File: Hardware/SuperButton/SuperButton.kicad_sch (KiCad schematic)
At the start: 0 parts

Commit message: Add switches
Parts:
- added C103: 5pf, Capacitor_SMD:C_0805_2012Metric, symbol Device:C_Small
- added C104: 0.1uf, Capacitor_SMD:C_0805_2012Metric, symbol Device:C_Small
- added D101, D102: 3.6 Zener, Diode_SMD:D_0805_2012Metric, symbol Device:D_Zener
- added D103: SDI, LED_SMD:LED_0805_2012Metric, symbol Device:LED
- added D104: PWR, LED_SMD:LED_0805_2012Metric, symbol Device:LED
- added J101: USBC, Connector_USB:USB_C_Receptacle_XKB_U262-16XN-4BVC11, symbol Connector:USB_C_Receptacle_USB2.0
- added J103: ICSP, Connector:Tag-Connect_TC2050-IDC-FP_2x05_P1.27mm_Vertical, symbol Connector_Generic:Conn_02x05_Odd_Even
- added R101, R102: 5K1, Resistor_SMD:R_0805_2012Metric, symbol Device:R_Small
- added R103, R105: 68R, Resistor_SMD:R_0805_2012Metric, symbol Device:R_Small
- added R104: 1K5, Resistor_SMD:R_0805_2012Metric, symbol Device:R_Small
- added R106, R107: 1K, Resistor_SMD:R_0805_2012Metric, symbol Device:R_Small
- added SW101: Switch, Switch_Keyboard_Cherry_MX:SW_Cherry_MX_PCB, symbol Switch:SW_SPST
- added U102: ATtiny85-20S, Package_SO:SOIC-8W_5.3x5.3mm_P1.27mm, symbol MCU_Microchip_ATtiny:ATtiny85-20S
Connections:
- new net: D103.1 (K), R106.2
- new net: J101.B5 (CC2), R101.2
- new net: J101.A5 (CC1), R102.2
- new net: D104.1 (K), R107.2
- new net +5V: C103.1, C104.1, D103.2 (A), D104.2 (A), J103.2 (Pin_2), R104.1, U102.8 (VCC)
- new net GND: C103.2, C104.2, D101.2 (A), D102.2 (A), J101.A1 (GND), J101.A12 (GND), J101.B1 (GND), J101.B12 (GND), J101.S1 (SHIELD), J103.10 (Pin_10), R101.1, R102.1, R107.1, SW101.2 (B), U102.4 (GND)
- new net ICSP_RST: J103.5 (Pin_5)
- new net RST: U102.1 (~{RESET}/PB5)
- new net SCK: J103.7 (Pin_7), SW101.1 (A), U102.7 (PB2)
- new net SDI: J103.9 (Pin_9), R106.1, U102.6 (PB1)
- new net SDO: J103.1 (Pin_1), U102.5 (AREF/PB0)
- new net USB+: D102.1 (K), J101.A6 (D+), J101.B6 (D+), R104.2, R105.1
- new net USB-: D101.1 (K), J101.A7 (D-), J101.B7 (D-), R103.1
- new net USBA: R105.2, U102.2 (XTAL1/PB3)
- new net USBB: R103.2, U102.3 (XTAL2/PB4)
- new net VBUS: J101.A4 (VBUS), J101.A9 (VBUS), J101.B4 (VBUS), J101.B9 (VBUS)
- no-connect marks 0 -> 6
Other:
- note added: "ICSP"
- note added: "LEDs"
- note added: "MCU"

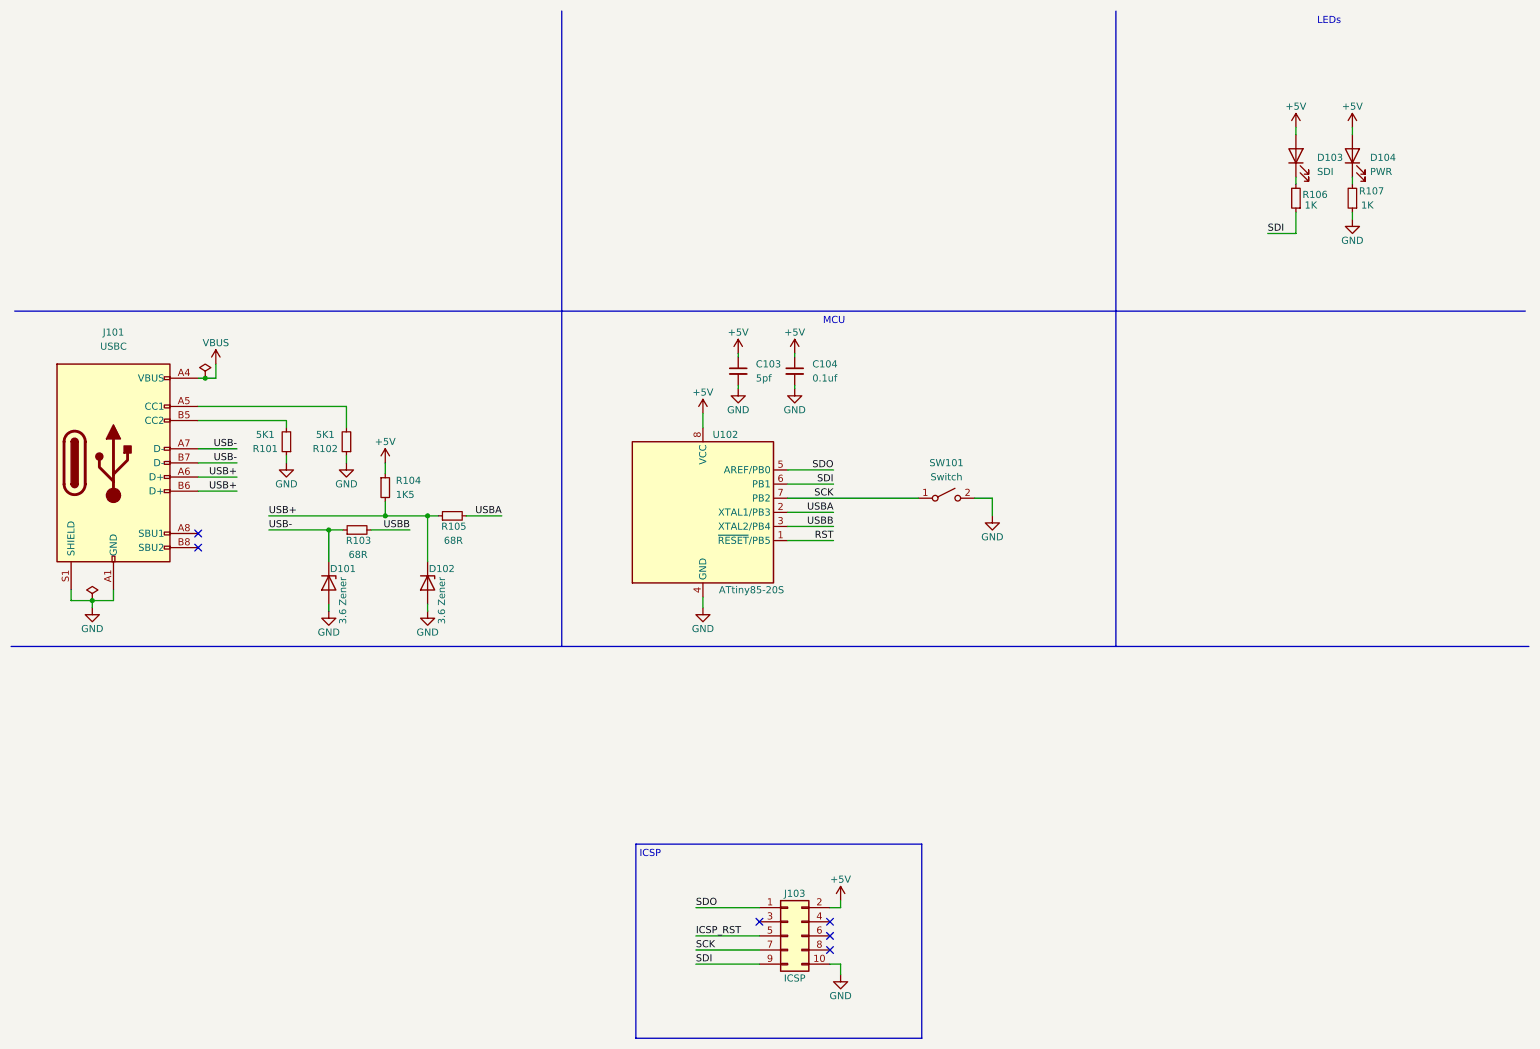
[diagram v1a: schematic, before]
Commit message: Add board outline
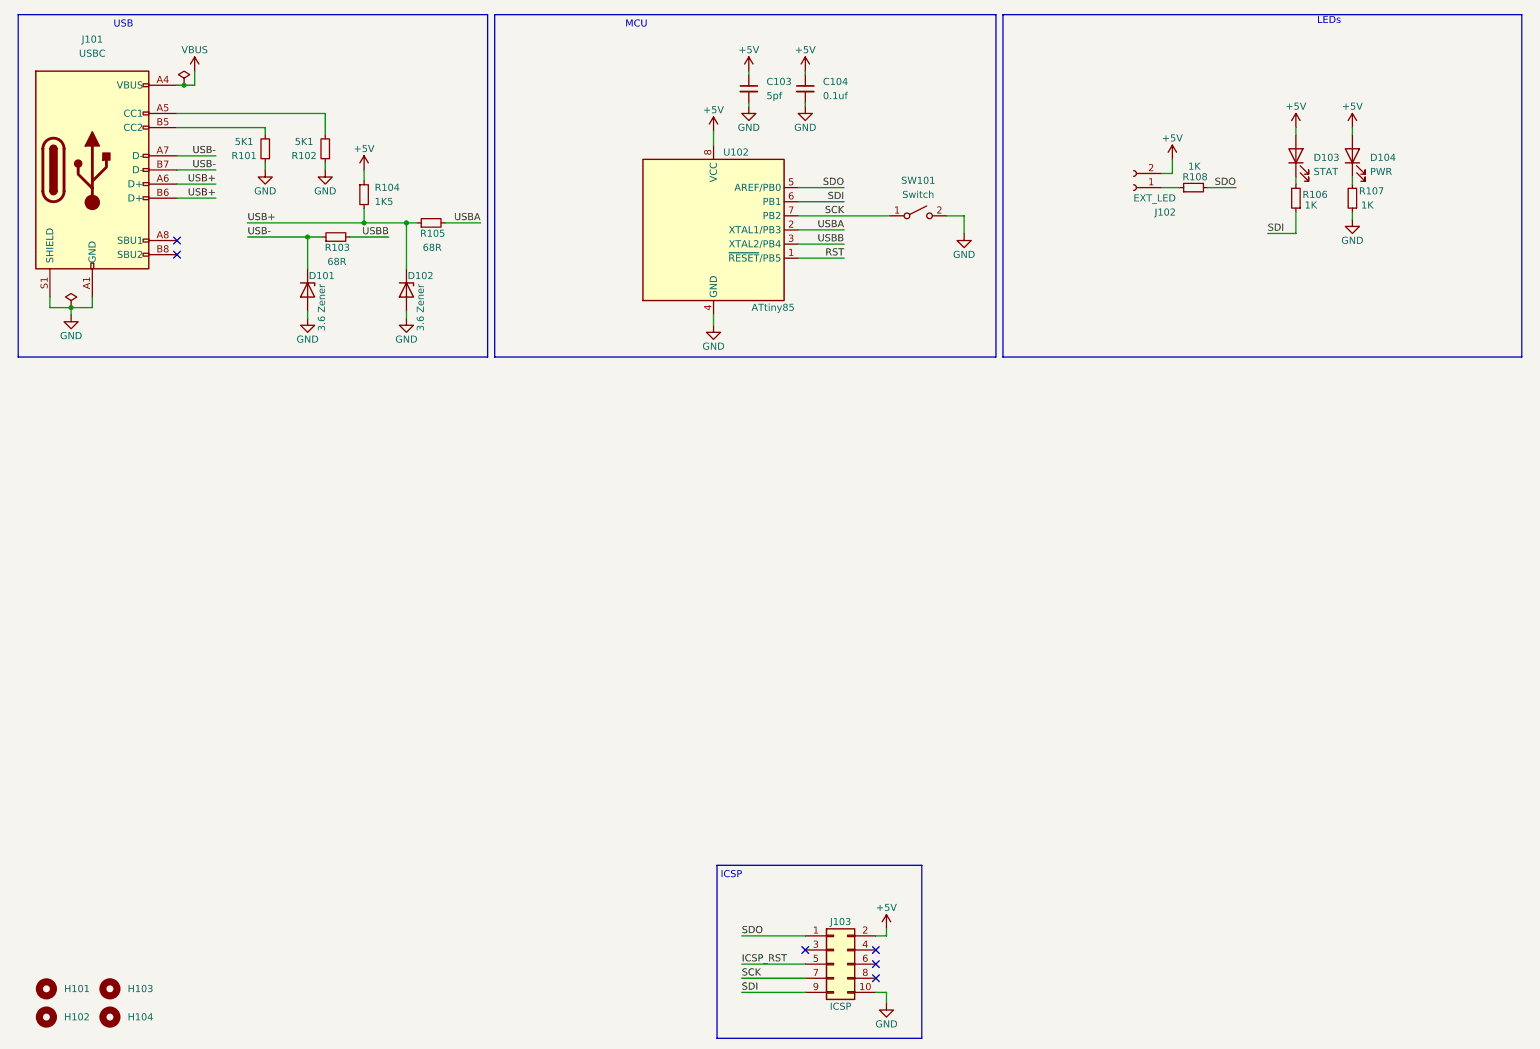
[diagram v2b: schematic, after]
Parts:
- added H101, H102, H103, H104: MountingHole, MountingHole:MountingHole_6.5mm, symbol Mechanical:MountingHole
- added J102: EXT_LED, Connector_Wire:SolderWire-0.15sqmm_1x02_P4mm_D0.5mm_OD1.5mm_Relief, symbol Connector:Conn_01x02_Female
- added R108: 1K, Resistor_SMD:R_0805_2012Metric, symbol Device:R_Small
- D103: value SDI -> STAT
- U102: value ATtiny85-20S -> ATtiny85
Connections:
- net +5V: now also J102.2 (Pin_2)
- net SDO: now also R108.2
- new net: J102.1 (Pin_1), R108.1
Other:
- note added: "USB"
- moved on the sheet: C103, C104, D101, D102, J101, J103, R101, R102, R103, R104, R105, SW101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

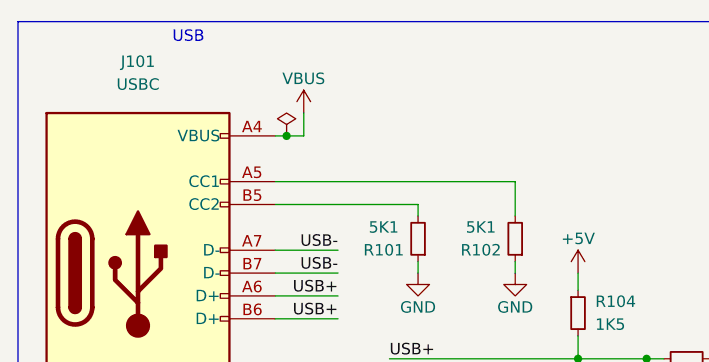
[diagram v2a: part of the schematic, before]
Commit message: Add ci/cd
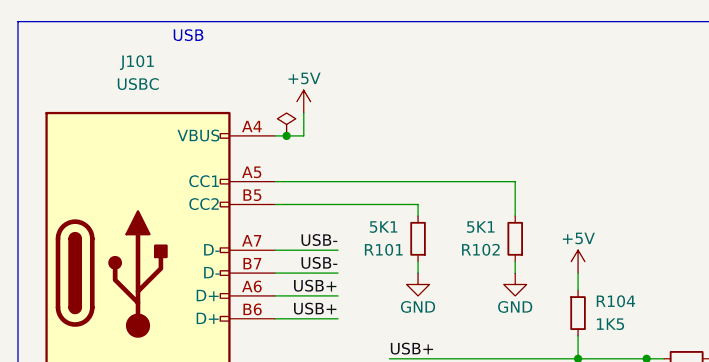
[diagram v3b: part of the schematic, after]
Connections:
- net VBUS is gone; now on net +5V: J101.A4 (VBUS), J101.A9 (VBUS), J101.B4 (VBUS), J101.B9 (VBUS)
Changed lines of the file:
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@@
+    (pin "1")
+  )
+  (symbol (lib_id "power:+5V") (at 45.085 23.495 0) (unit 1)
+    (in_bom yes) (on_board yes)
+    (property "Reference" "#PWR?" (id 0) (at 45.085 27.305 0)
+      (effects (font (size 1.27 1.27)) hide)
+    )
+    (property "Value" "+5V" (id 1) (at 45.085 19.685 0))
+    (property "Footprint" "" (id 2) (at 45.085 23.495 0)
+      (effects (font (size 1.27 1.27)) hide)
+    )
+    (property "Datasheet" "" (id 3) (at 45.085 23.495 0)
+      (effects (font (size 1.27 1.27)) hide)
+    )
     (pin "1")
   )
@@
     )
     (property "Datasheet" "" (id 3) (at 83.185 67.945 0)
-      (effects (font (size 1.27 1.27)) hide)
-    )
-    (pin "1")
-  )
-  (symbol (lib_id "power:VBUS") (at 45.085 23.495 0) (unit 1)
-    (in_bom yes) (on_board yes)
-    (property "Reference" "#PWR0117" (id 0) (at 45.085 27.305 0)
-      (effects (font (size 1.27 1.27)) hide)
-    )
-    (property "Value" "VBUS" (id 1) (at 45.085 19.685 0))
-    (property "Footprint" "" (id 2) (at 45.085 23.495 0)
-      (effects (font (size 1.27 1.27)) hide)
-    )
-    (property "Datasheet" "" (id 3) (at 45.085 23.495 0)
       (effects (font (size 1.27 1.27)) hide)
     )
@@
       (reference "#PWR0116") (unit 1) (value "GND") (footprint "")
     )
-    (path "/24487fac-3471-4a2e-a636-bc4b8b05c989"
-      (reference "#PWR0117") (unit 1) (value "VBUS") (footprint "")
-    )
     (path "/e8def7ce-3c91-44dc-84e6-03f70fae4ce8"
       (reference "#PWR0118") (unit 1) (value "GND") (footprint "")
@@
       (reference "#PWR0121") (unit 1) (value "+5V") (footprint "")
     )
+    (path "/05f1f0c0-1fb1-4746-8d9b-f5d06dd44701"
+      (reference "#PWR?") (unit 1) (value "+5V") (footprint "")
+    )
     (path "/ec261643-1568-4081-bb06-d04055847d6b"

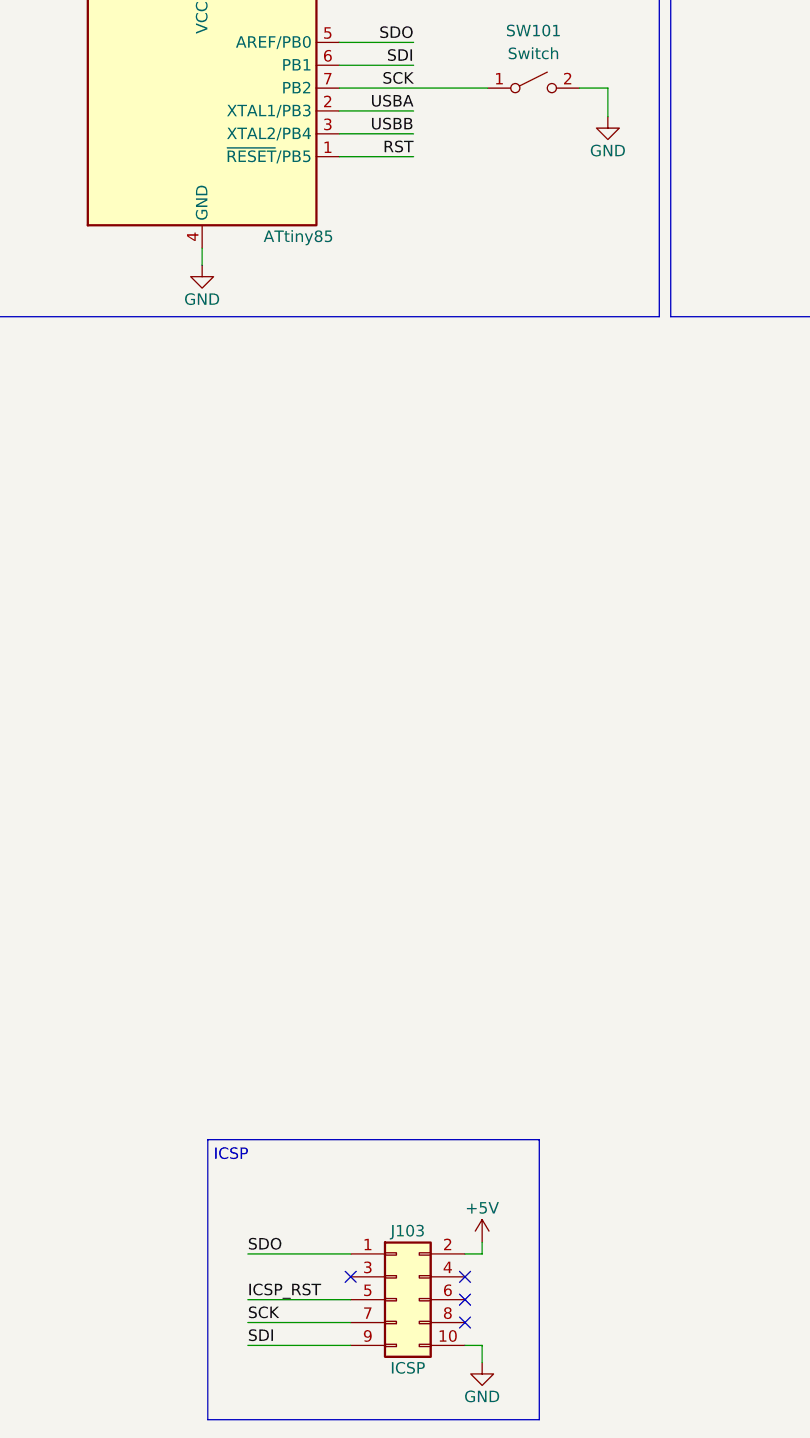
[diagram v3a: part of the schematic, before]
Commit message: Add reset pullups
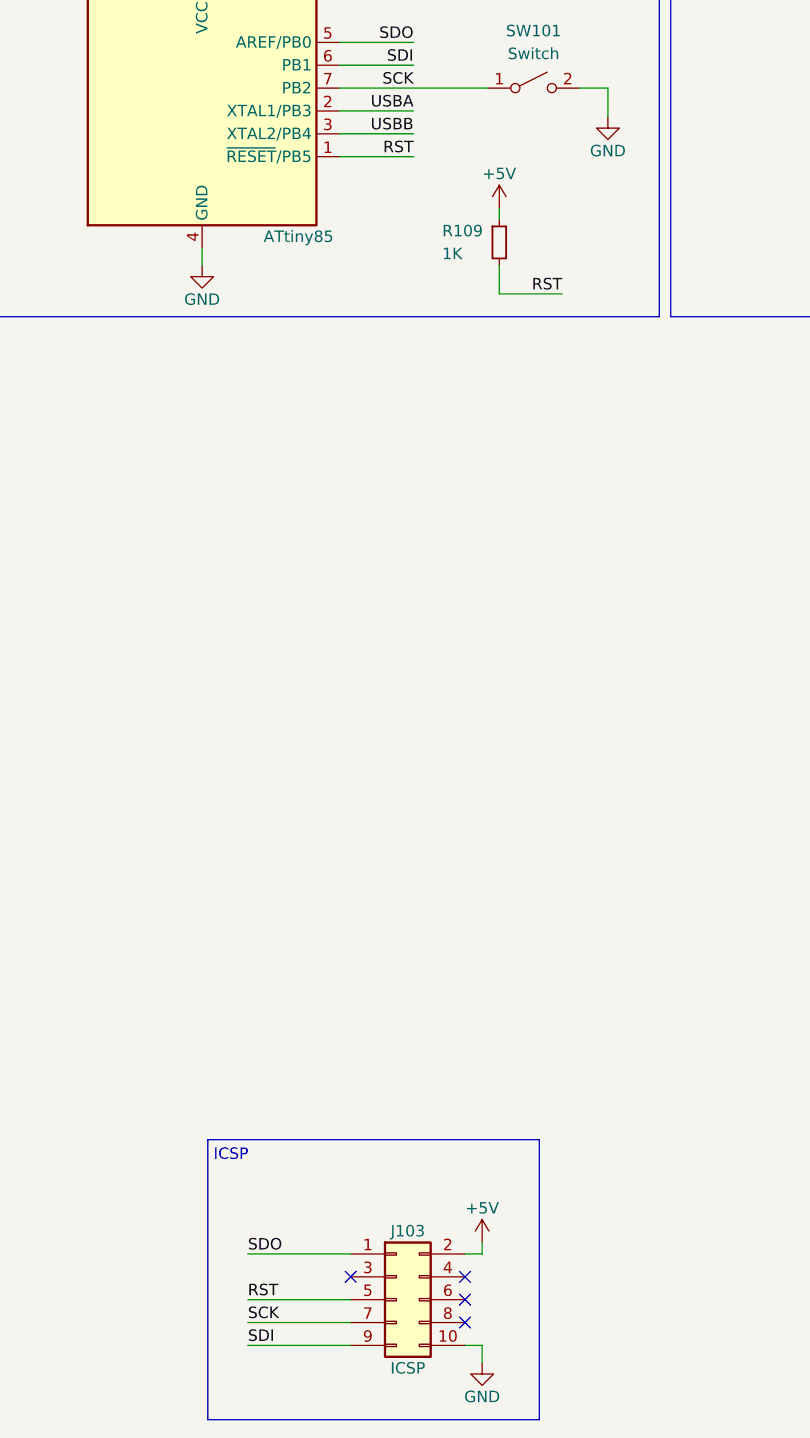
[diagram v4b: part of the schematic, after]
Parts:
- added R109: 1K, Resistor_SMD:R_0805_2012Metric, symbol Device:R_Small
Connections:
- net ICSP_RST is gone; now on net RST: J103.5 (Pin_5)
- net +5V: now also R109.1
- net RST: now also R109.2
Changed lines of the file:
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@@
+    (stroke (width 0) (type default) (color 0 0 0 0))
+  )
+  (wire (pts (xy 171.45 62.865) (xy 171.45 64.135))
     (stroke (width 0) (type default) (color 0 0 0 0))
   )
@@
     (stroke (width 0) (type default) (color 0 0 0 0))
   )
+  (wire (pts (xy 171.45 72.39) (xy 171.45 69.215))
+    (stroke (width 0) (type default) (color 0 0 0 0))
+  )
   (wire (pts (xy 26.67 66.04) (xy 26.67 64.135))
     (stroke (width 0) (type default) (color 0 0 0 0))
@@
   )
   (polyline (pts (xy 189.23 13.335) (xy 189.23 74.93))
+    (stroke (width 0) (type default) (color 0 0 0 0))
+  )
+  (wire (pts (xy 178.435 72.39) (xy 171.45 72.39))
     (stroke (width 0) (type default) (color 0 0 0 0))
   )
@@
     (effects (font (size 1.27 1.27)) (justify left bottom))
   )
-  (label "ICSP_RST" (at 143.51 184.15 0)
+  (label "RST" (at 143.51 184.15 0)
     (effects (font (size 1.27 1.27)) (justify left bottom))
   )
@@
   )
   (label "USB-" (at 48.895 41.275 180)
+    (effects (font (size 1.27 1.27)) (justify right bottom))
+  )
+  (label "RST" (at 178.435 72.39 180)
     (effects (font (size 1.27 1.27)) (justify right bottom))
   )
@@
   (symbol (lib_id "power:+5V") (at 45.085 23.495 0) (unit 1)
     (in_bom yes) (on_board yes)
-    (property "Reference" "#PWR?" (id 0) (at 45.085 27.305 0)
+    (property "Reference" "#PWR0113" (id 0) (at 45.085 27.305 0)
       (effects (font (size 1.27 1.27)) hide)
     )
@@
     (pin "2")
   )
+  (symbol (lib_id "Device:R_Small") (at 171.45 66.675 0) (unit 1)
+    (in_bom yes) (on_board yes)
+    (property "Reference" "R109" (id 0) (at 165.1 65.405 0)
+      (effects (font (size 1.27 1.27)) (justify left))
+    )
+    (property "Value" "1K" (id 1) (at 165.1 67.945 0)
+      (effects (font (size 1.27 1.27)) (justify left))
+    )
+    (property "Footprint" "Resistor_SMD:R_0805_2012Metric" (id 2) (at 171.45 66.675 0)
+      (effects (font (size 1.27 1.27)) hide)
+    )
+    (property "Datasheet" "~" (id 3) (at 171.45 66.675 0)
+      (effects (font (size 1.27 1.27)) hide)
+    )
+    (pin "1")
+    (pin "2")
+  )
+  (symbol (lib_id "power:+5V") (at 171.45 62.865 0) (unit 1)
+    (in_bom yes) (on_board yes)
+    (property "Reference" "#PWR0117" (id 0) (at 171.45 66.675 0)
+      (effects (font (size 1.27 1.27)) hide)
+    )
+    (property "Value" "+5V" (id 1) (at 171.45 59.055 0))
+    (property "Footprint" "" (id 2) (at 171.45 62.865 0)
+      (effects (font (size 1.27 1.27)) hide)
+    )
+    (property "Datasheet" "" (id 3) (at 171.45 62.865 0)
+      (effects (font (size 1.27 1.27)) hide)
+    )
+    (pin "1")
+  )
   (symbol (lib_id "power:+5V") (at 253.365 33.655 0) (unit 1)
     (in_bom yes) (on_board yes)
@@
       (reference "#PWR0112") (unit 1) (value "+5V") (footprint "")
     )
+    (path "/05f1f0c0-1fb1-4746-8d9b-f5d06dd44701"
+      (reference "#PWR0113") (unit 1) (value "+5V") (footprint "")
+    )
     (path "/9e36bade-b0c8-4ce8-b918-646bbadc881e"
       (reference "#PWR0114") (unit 1) (value "GND") (footprint "")
@@
       (reference "#PWR0116") (unit 1) (value "GND") (footprint "")
     )
+    (path "/e2811b4e-0103-43d7-838d-0e0e0bfb4731"
+      (reference "#PWR0117") (unit 1) (value "+5V") (footprint "")
+    )
     (path "/e8def7ce-3c91-44dc-84e6-03f70fae4ce8"
       (reference "#PWR0118") (unit 1) (value "GND") (footprint "")
@@
       (reference "#PWR0121") (unit 1) (value "+5V") (footprint "")
     )
-    (path "/05f1f0c0-1fb1-4746-8d9b-f5d06dd44701"
-      (reference "#PWR?") (unit 1) (value "+5V") (footprint "")
-    )
     (path "/ec261643-1568-4081-bb06-d04055847d6b"
       (reference "C103") (unit 1) (value "5pf") (footprint "Capacitor_SMD:C_0805_2012Metric")
@@
       (reference "R108") (unit 1) (value "1K") (footprint "Resistor_SMD:R_0805_2012Metric")
     )
+    (path "/e0f6f7d4-f858-4b00-af7d-d060c39d7c41"
+      (reference "R109") (unit 1) (value "1K") (footprint "Resistor_SMD:R_0805_2012Metric")
+    )
     (path "/b8d5b78d-bdc1-4b0f-aeef-2faded5aec7d"
